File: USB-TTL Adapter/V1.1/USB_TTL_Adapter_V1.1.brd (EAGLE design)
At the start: 100 x 100 mm, 4 parts, among them X1 22-23-2041, X3 22-23-2041

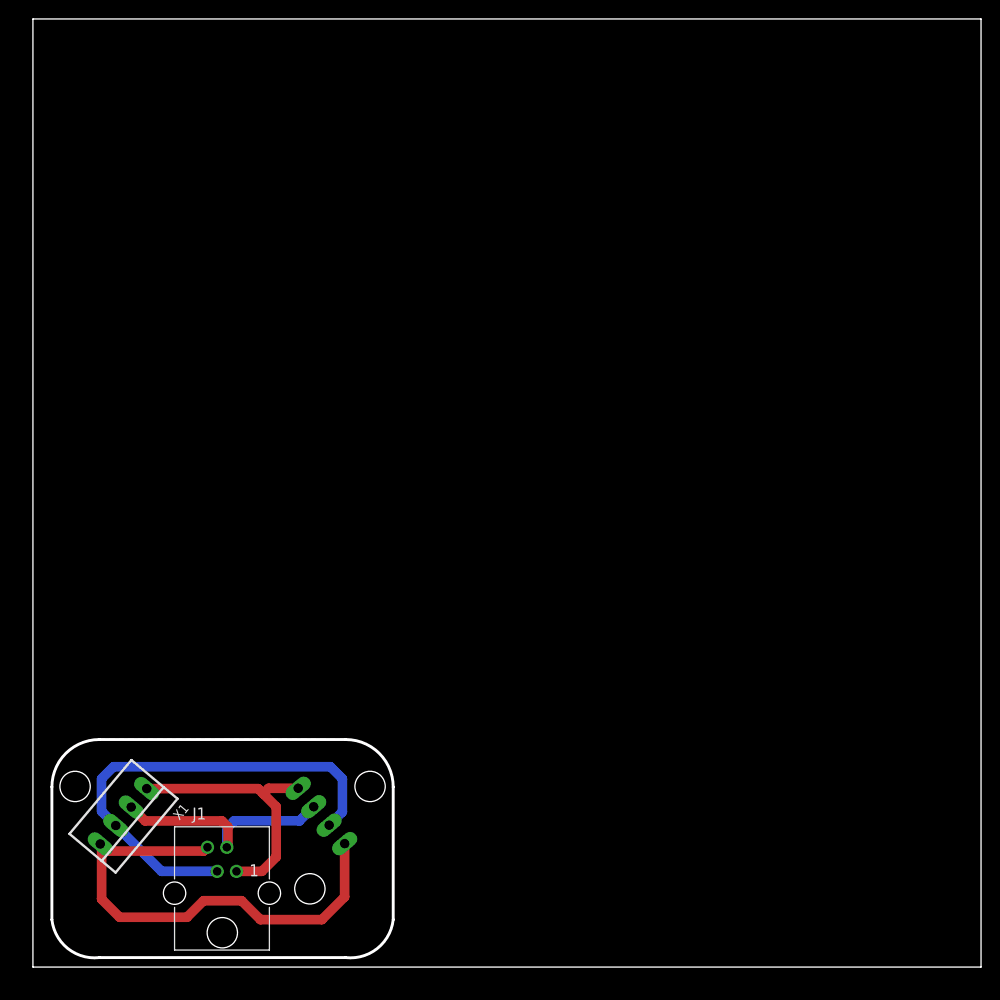
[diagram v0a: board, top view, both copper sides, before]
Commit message: 
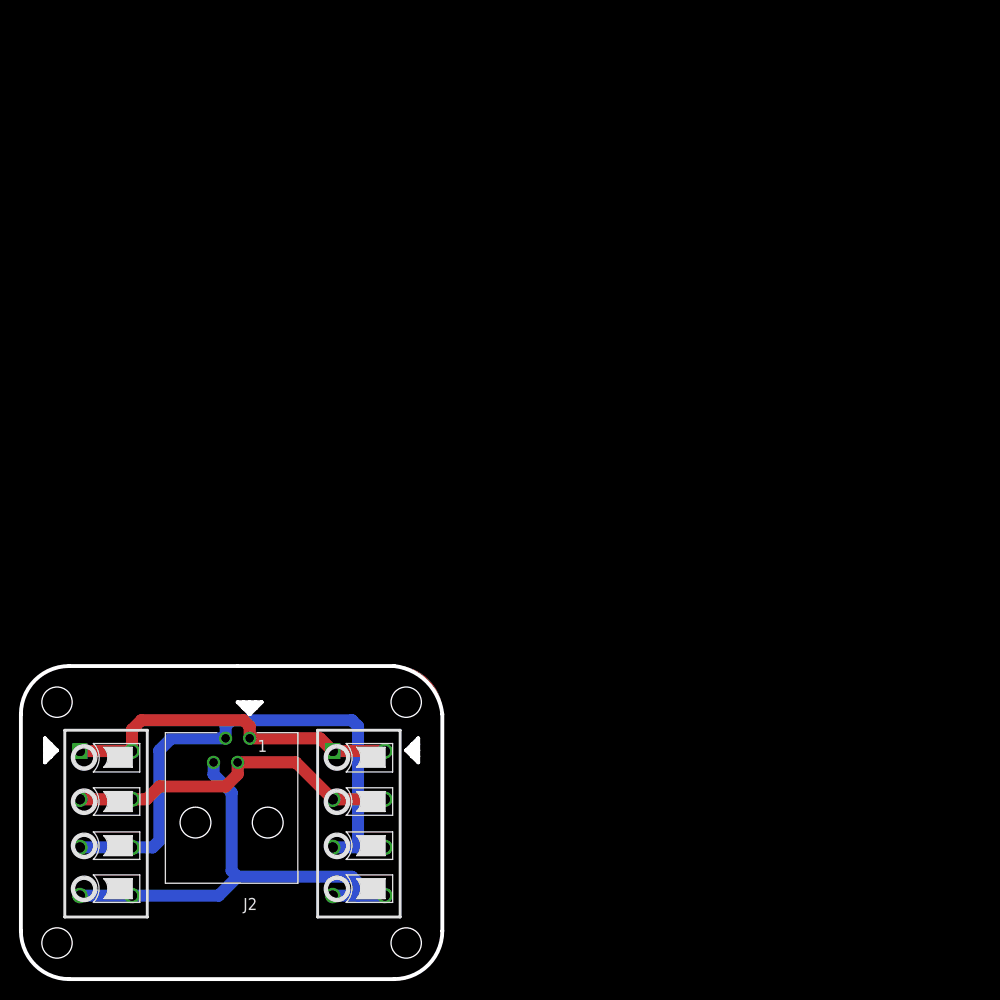
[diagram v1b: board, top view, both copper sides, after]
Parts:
- removed E$1: (no value), !!!Platinen_Logo!!!:25X25_BEST
- removed J1: (no value), InputOutputIO (rev18b):615004143821
- removed X1, X3: 22-23-2041, con-molex:22-23-2041
- added J2: (no value), InputOutputIO (rev18b):615004144021
- added U$1: (no value), !!!Platinen_Logo!!!:25X25_BEST
- added XK1, XK2: FKK_4/5.08_LSFSMT5.08/04/1803.5SNBKTU, Federkraftklemme - LSF-SMT5.08:LSF4
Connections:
- net N$1: now also J2.4, XK1.4, XK1.4.1, XK2.4, XK2.4.1; no longer J1.1, X1.1, X3.1
- net N$2: now also J2.3, XK1.3, XK1.3.1, XK2.3, XK2.3.1; no longer J1.2, X1.2, X3.2
- net N$3: now also J2.2, XK1.2, XK1.2.1, XK2.2, XK2.2.1; no longer J1.3, X1.3, X3.3
- net N$4: now also J2.1, XK1.1, XK1.1.1, XK2.1, XK2.1.1; no longer J1.4, X1.4, X3.4
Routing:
- net N$2: track 25.4 -> 59.8 mm
- net N$1: track 28.5 -> 50.4 mm
- net N$4: track 52.3 -> 36.9 mm
- net N$3: track 50.2 -> 36.1 mm
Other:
- board size 100 x 100 mm -> 44.5 x 33 mm

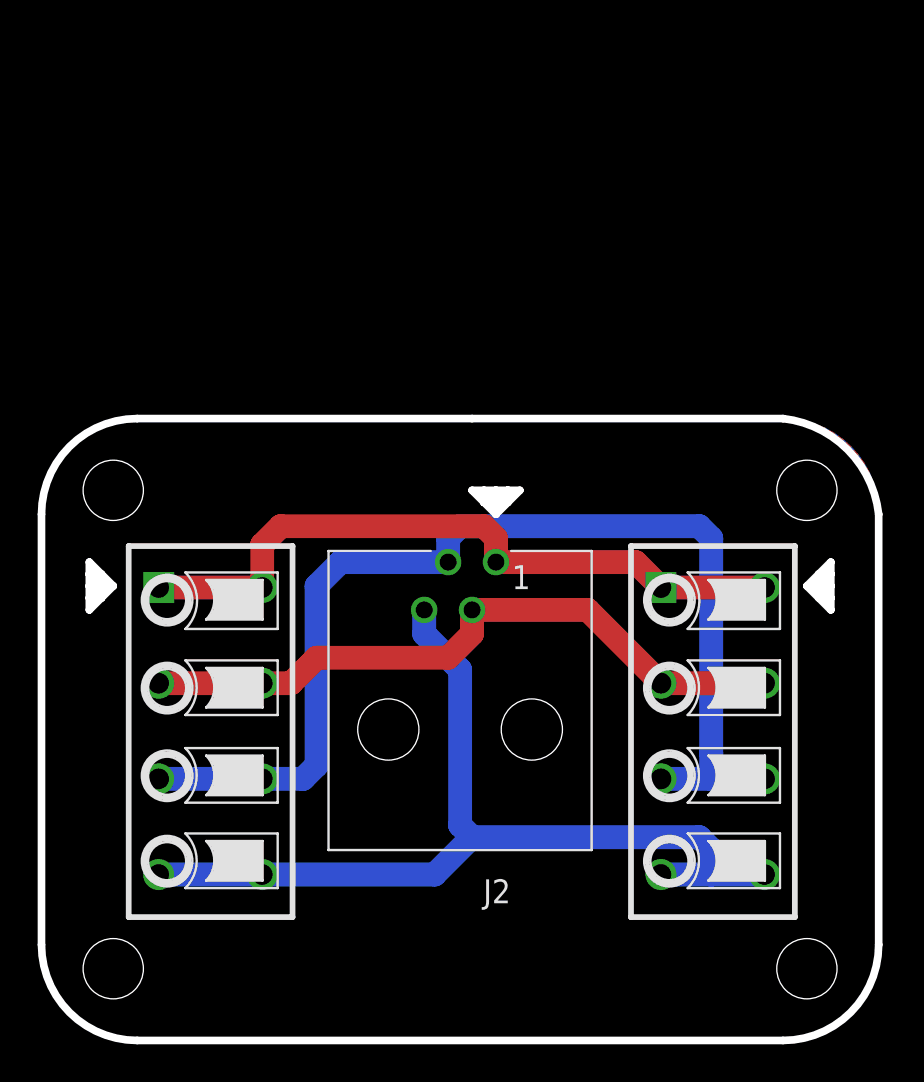
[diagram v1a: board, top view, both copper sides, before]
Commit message: 
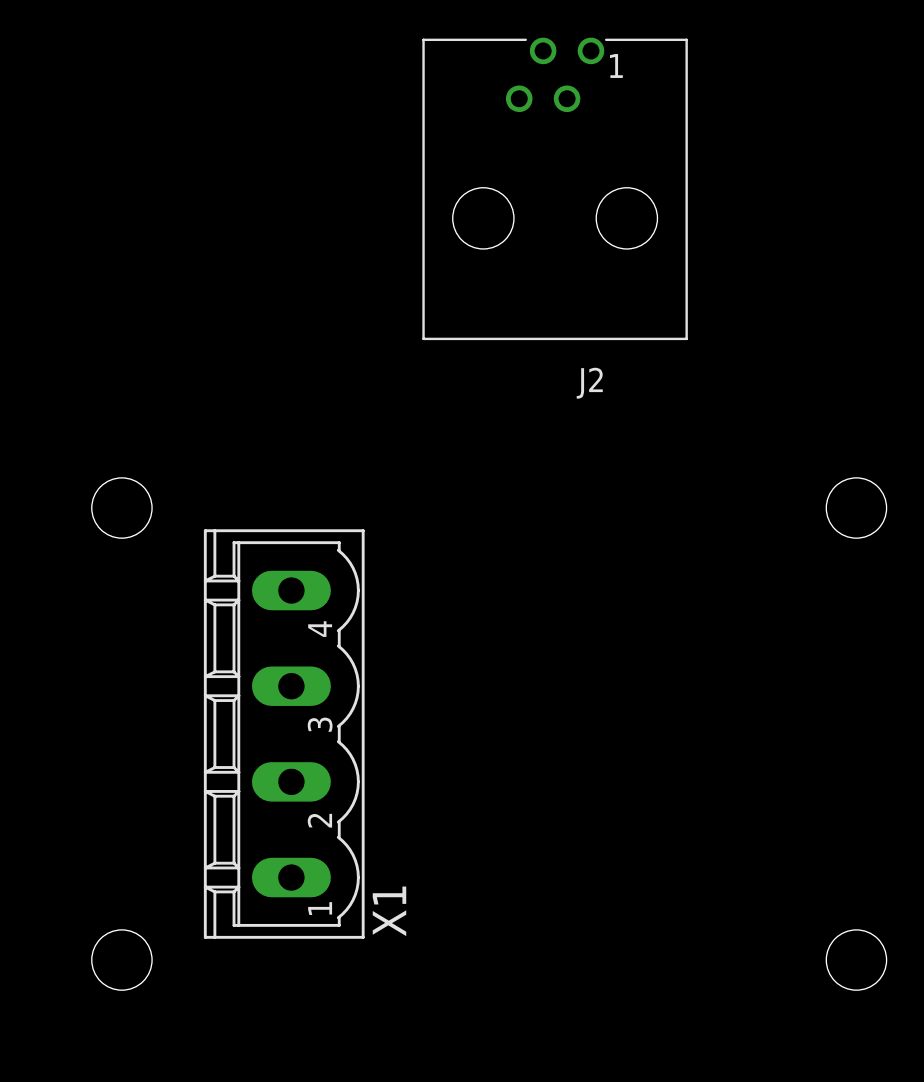
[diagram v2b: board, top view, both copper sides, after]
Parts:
- removed XK1, XK2: FKK_4/5.08_LSFSMT5.08/04/1803.5SNBKTU, Federkraftklemme - LSF-SMT5.08:LSF4
- added X1: MSTBV4, con-phoenix-508:MSTBV4
- moved U$1 134.0 mm to (127.0, 85.8)
- moved J2 27.6 mm to (26.0, 50.0)
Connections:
- net N$1: now also X1.4; no longer XK1.4, XK1.4.1, XK2.4, XK2.4.1
- net N$2: now also X1.3; no longer XK1.3, XK1.3.1, XK2.3, XK2.3.1
- net N$3: now also X1.2; no longer XK1.2, XK1.2.1, XK2.2, XK2.2.1
- net N$4: now also X1.1; no longer XK1.1, XK1.1.1, XK2.1, XK2.1.1
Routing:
- net N$2: track 59.8 -> 0.00 mm
- net N$1: track 50.4 -> 0.00 mm
- net N$4: track 36.9 -> 0.00 mm
- net N$3: track 36.1 -> 0.00 mm
- removed copper zone on layer 1, net GND
- removed copper zone on layer 16, net GND
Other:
- board outline removed

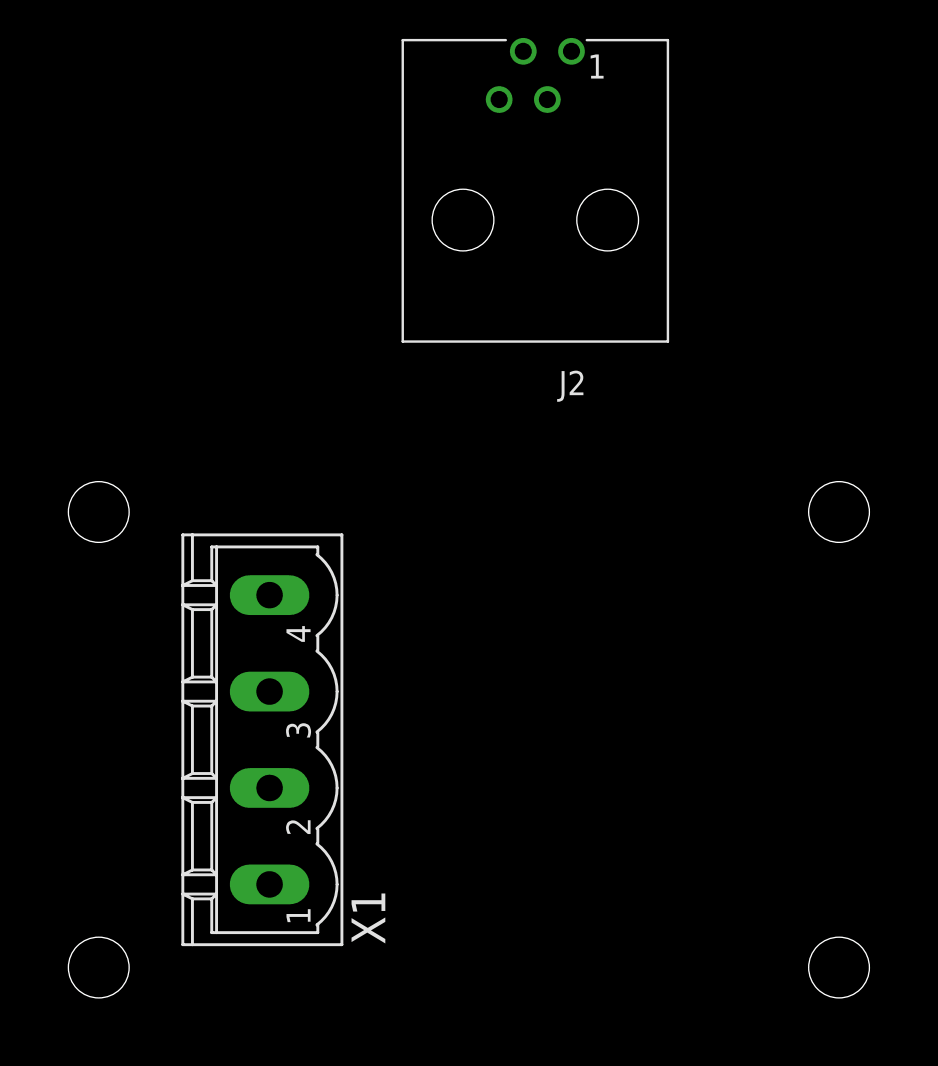
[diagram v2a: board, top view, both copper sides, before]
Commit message: 
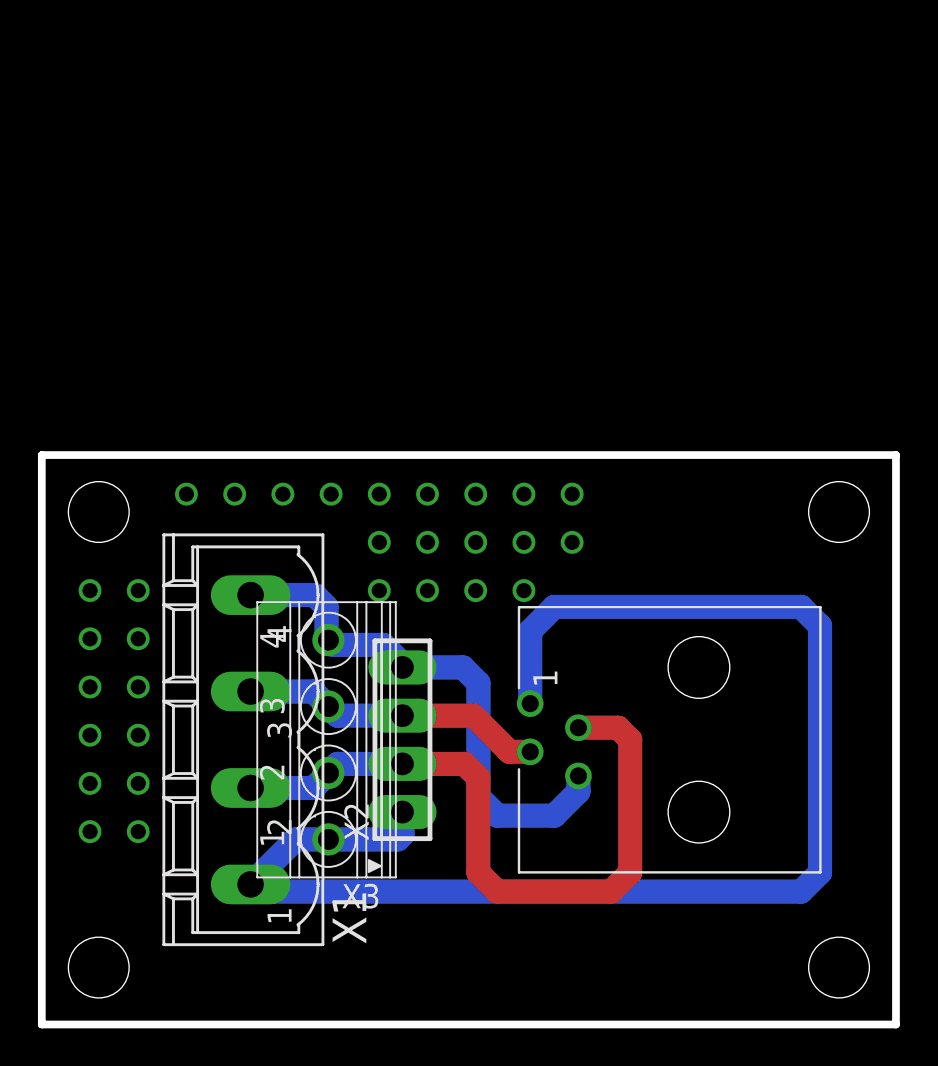
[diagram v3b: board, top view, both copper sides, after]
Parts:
- added X2: (no value), con-phoenix-254:4POL254
- added X3: 1751264, con-phoenix-350:1751264
- moved U$1 133.3 mm to (21.4, 4.40), turned to 10 degrees
- moved J2 35.0 mm to (27.0, 15.0), turned to 270 degrees
- moved X1 1.00 mm to (11.0, 15.0)
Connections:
- net N$1: now also X2.4, X3.4
- net N$2: now also X2.3, X3.3
- net N$3: now also X2.2, X3.2
- net N$4: now also X2.1, X3.1
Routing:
- net N$4: track 0.00 -> 73.9 mm
- net N$3: track 0.00 -> 36.6 mm
- net N$1: track 0.00 -> 28.0 mm
- net N$2: track 0.00 -> 16.0 mm
- added copper zone on layer 1, net GND
- added copper zone on layer 16, net GND
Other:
- board outline added: 45 x 30 mm
- board text added: "1: VCC"
- board text added: "2: GND"
- board text added: "3: RxD"
- board text added: "4: TxD"
